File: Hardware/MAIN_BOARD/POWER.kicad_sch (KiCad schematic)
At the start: 149 parts, among them J12 Conn_01x02, J17 Conn_01x02, J18 Conn_01x02, Q1 IRFR120N, Q2 IRFR120N, Q3 MJD44H11, Q4 MJD44H11, T1 Transformer_1P_2S, U12 LT3042xMSE, U12 TPS562201DDCR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

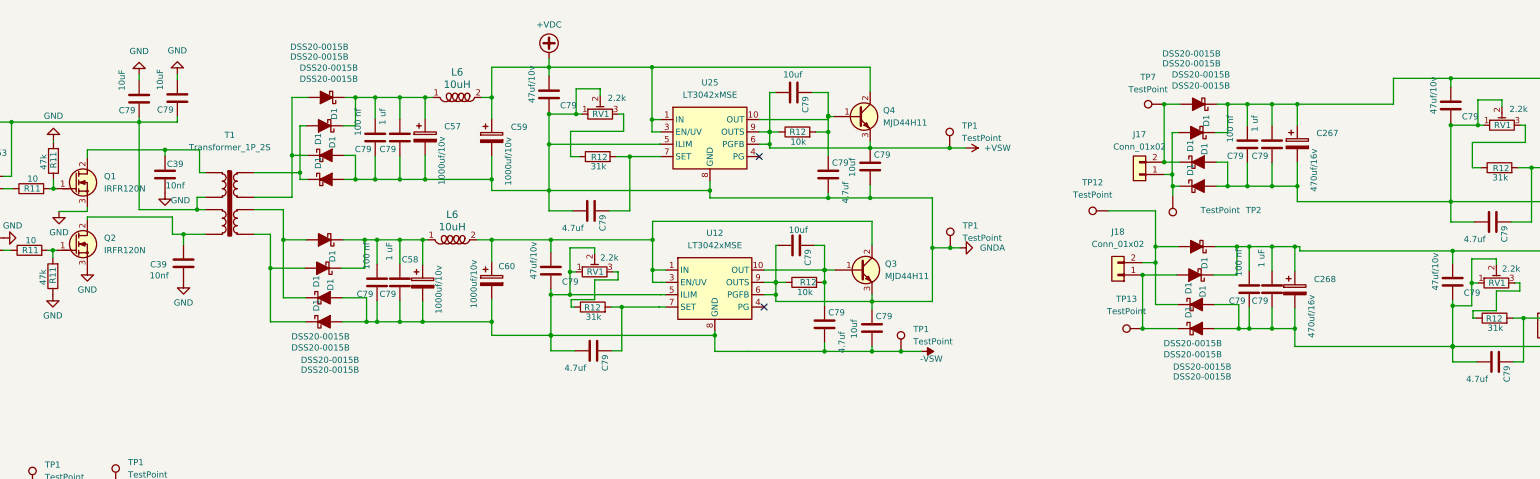
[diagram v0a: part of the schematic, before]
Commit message: some PCB/schemtic improvements
some PCB improvements,
three additional debug LEDs,
add serial res. at data/clk line
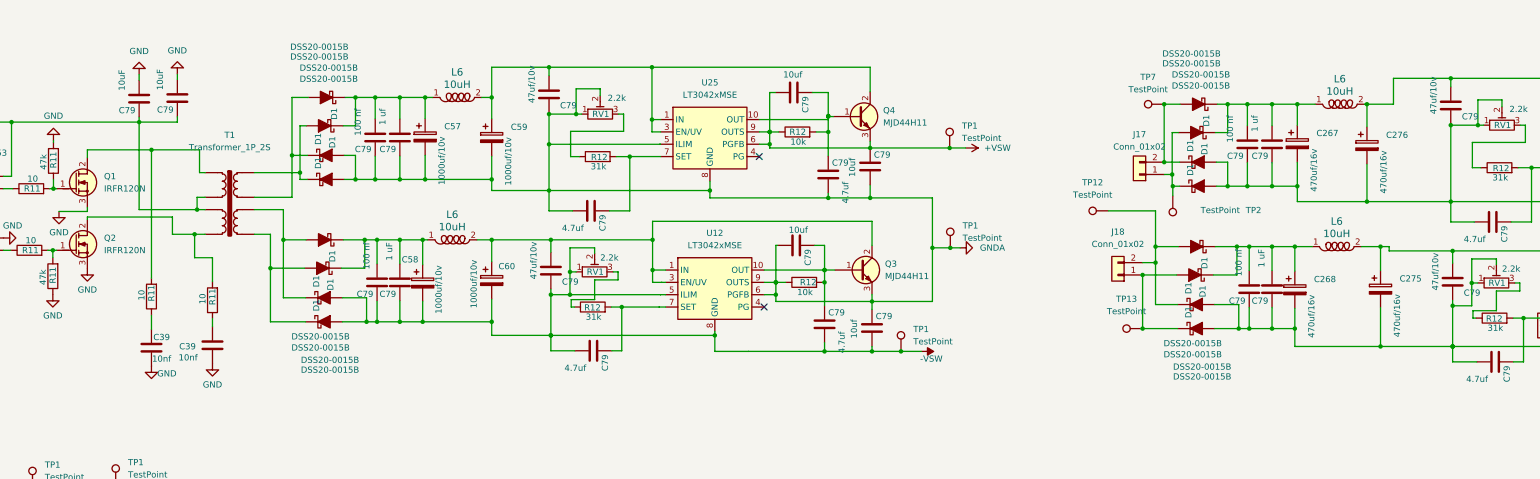
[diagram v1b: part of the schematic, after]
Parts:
- added C275, C276: 470uf/16v, PCM_Capacitor_THT_AKL:CP_Radial_D10.0mm_P3.50mm, symbol PCM_Capacitor_AKL:CP_Radial_D8.0mm_P2.50mm
- added L6 (x2): 10uH, Inductor_SMD:L_Coilcraft_LPS5030, symbol dk_Fixed-Inductors:82103C
- added R11 (x2): 10, PCM_Resistor_SMD_AKL:R_1812_4532Metric, symbol Erdal:R_0603
- C267, C268, C57, C58, C59, C60: footprint PCM_Capacitor_THT_AKL:CP_Radial_D10.0mm_P5.00mm -> PCM_Capacitor_THT_AKL:CP_Radial_D10.0mm_P3.50mm
- L1: footprint Inductor_SMD:L_Coilcraft_LPS3314 -> Inductor_SMD:L_Coilcraft_LPS4018
- L6: footprint Inductor_SMD:L_Coilcraft_LPS4018 -> Inductor_SMD:L_Coilcraft_LPS5030
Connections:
- net -15V: now also C275.2
- net GNDA: now also C276.2
- net at C267.1, C79.2, C79.2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: now also L6.1; no longer C79.2, U69.1 (IN), U69.2 (IN), U69.3 (EN/UV), U69.6 (PGFB)
- net at Q1.2 (D), T1.1: now also R11.2; no longer C39.1
- net at Q2.2 (D), T1.4: now also R11.2; no longer C39.1
- net at C268.1, C79.2, C79.2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: now also L6.1; no longer C79.2, U70.1 (IN), U70.2 (IN), U70.3 (EN/UV), U70.6 (PGFB)
- net +VDC: no longer names the net of C59.1, C79.2, L6.2, Q4.2 (C), U25.1 (IN), U25.2 (IN), U25.3 (EN/UV)
- new net: C276.1, C79.2, L6.2, U69.1 (IN), U69.2 (IN), U69.3 (EN/UV), U69.6 (PGFB)
- new net: C39.1, R11.1 (x2)
- new net: C275.1, C79.2, L6.2, U70.1 (IN), U70.2 (IN), U70.3 (EN/UV), U70.6 (PGFB)
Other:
- moved on the sheet: C39
